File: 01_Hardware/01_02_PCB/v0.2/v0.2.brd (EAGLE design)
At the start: 160 x 100 mm, 57 parts

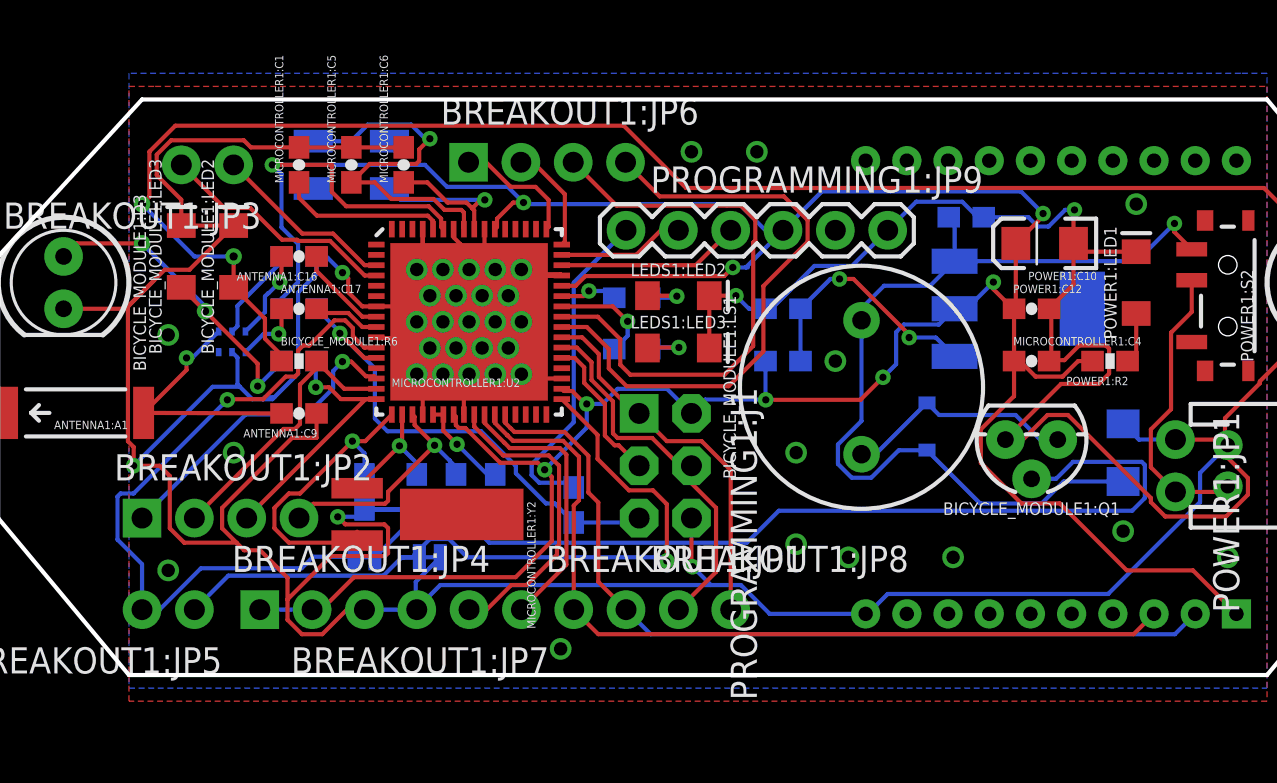
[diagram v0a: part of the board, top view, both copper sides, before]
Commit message: v0.2 updates (minor traces), readme updates
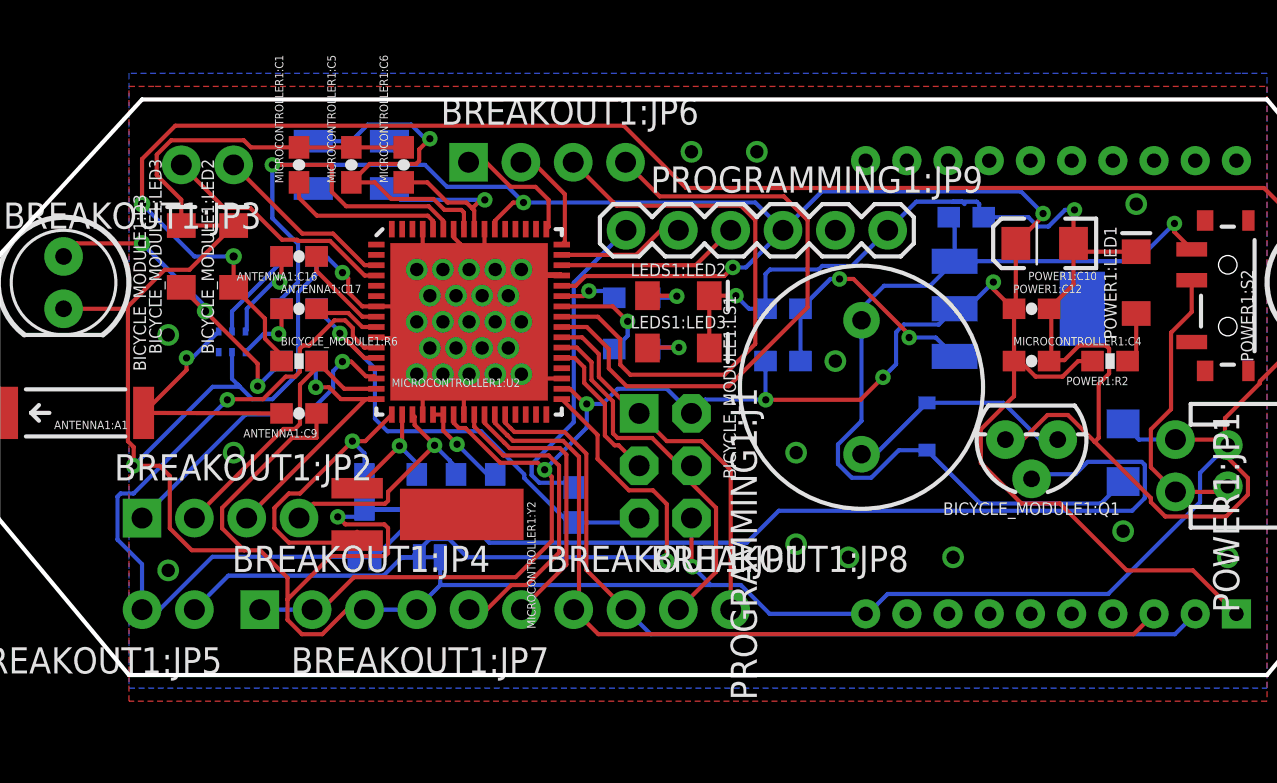
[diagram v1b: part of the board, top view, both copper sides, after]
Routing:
- net GND: track 305.8 -> 302.9 mm, vias 43 -> 42
